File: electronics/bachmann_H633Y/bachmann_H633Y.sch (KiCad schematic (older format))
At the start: 27 parts

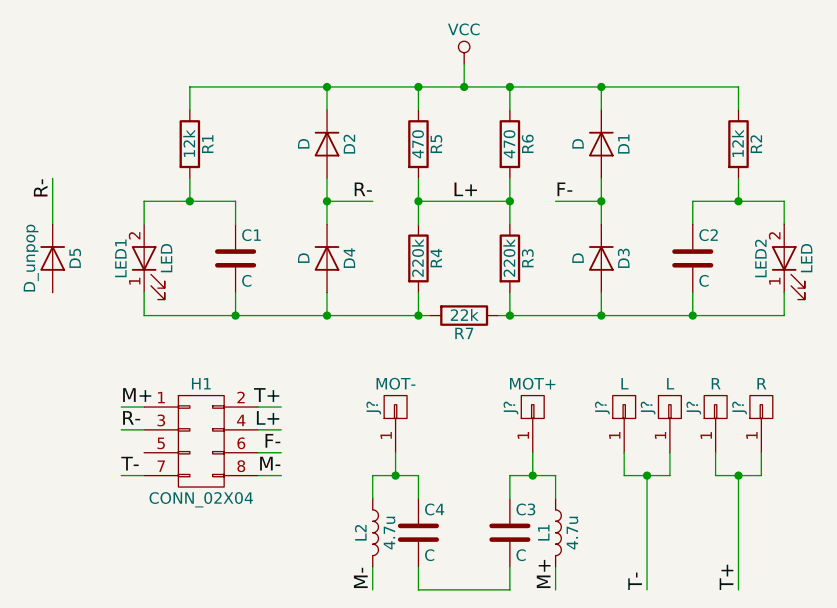
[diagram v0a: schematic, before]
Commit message: electronics: Re-label Bachmann L+ to Io
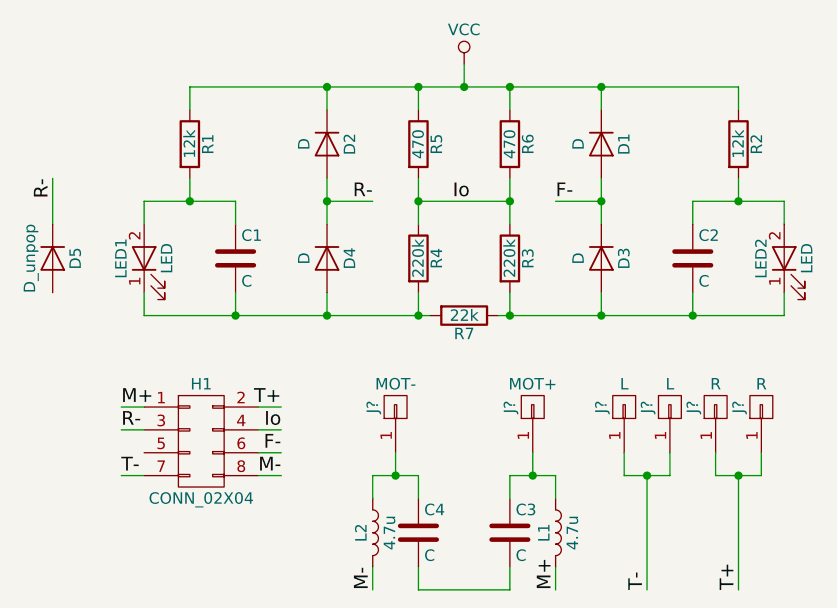
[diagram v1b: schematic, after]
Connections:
- net L+ renamed Io
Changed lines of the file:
@@
 LIBS:contrib
 LIBS:valves
-LIBS:locomotive_bachmann-cache
+LIBS:bachmann_H633Y-cache
 EELAYER 25 0
 EELAYER END
@@
 M-
 Text Label 5100 4800 2    60   ~ 0
-L+
+Io
 Text Label 5100 4900 2    60   ~ 0
 F-
@@
 $EndComp
 Text Label 5850 3800 0    60   ~ 0
-L+
+Io
 Text Label 7100 5500 1    60   ~ 0
 T+
